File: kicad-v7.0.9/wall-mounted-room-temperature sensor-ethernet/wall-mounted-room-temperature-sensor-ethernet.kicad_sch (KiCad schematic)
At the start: 165 parts, among them J1 54601-908WPLF, P1 2x3_MLW06A, P2 DS1023-1-9S21, Q1 DMG2307L, Q2 FDC2512, SW1 TVAF18BB, SW2 TVAF18BB, SW3 B3F-4150, SW4 B3F-4150, SW5 B3F-4150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

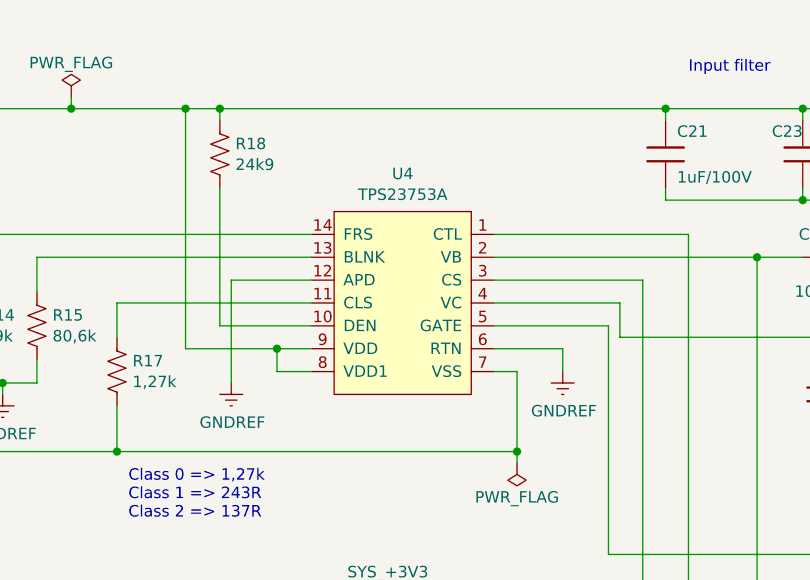
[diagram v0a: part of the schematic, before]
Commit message: Change components form library. Adding of BOM.
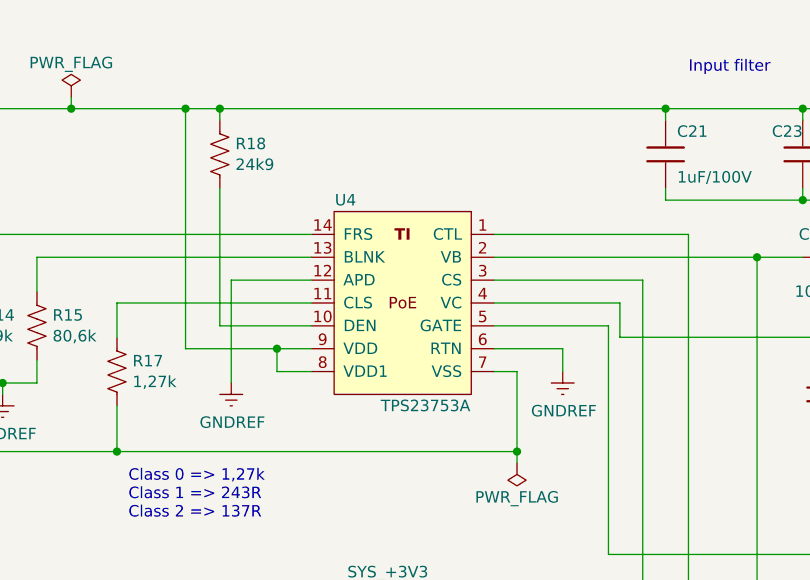
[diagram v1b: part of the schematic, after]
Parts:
- P1: footprint connector_idc_rl:2x3_MLW06A -> connector_idc_tht_rl:2x3_MLW06A; symbol connector_idc_rl:2x3_MLW06A -> connector_idc_tht_rl:2x3_MLW06A
- P2: footprint connector_tht_pinsocket_2.54mm_rl:1x9_pinsocket_2.54mm_vertical_8.5mm -> connector_pin_socket_2.54mm_tht_rl:1x9_pin_socket_2.54mm_vertical_8.5mm; symbol connector_tht_pin_socket_2.54mm_rl:DS1023-1-9S21 -> connector_pin_socket_2.54mm_tht_rl:DS1023-1-9S21
- U4: symbol poe_interface_isolated_converter_rl:TPS23753A -> poe_interface_isolated_converter_rl:TPS23753APW
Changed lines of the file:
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@@
     (effects (font (size 1.27 1.27)) (justify left bottom))
   )
-  (symbol (lib_id "poe_interface_isolated_converter_rl:TPS23753A") (at 168.91 57.15 0) (mirror y) (unit 1)
+  (symbol (lib_id "poe_interface_isolated_converter_rl:TPS23753APW") (at 168.91 57.15 0) (mirror y) (unit 1)
     (in_bom yes) (on_board yes) (dnp no)
-    (property "Reference" "U4" (at 168.91 40.259 0)
+    (property "Reference" "U4" (at 162.56 43.18 0)
       (effects (font (size 1.27 1.27)))
     )
-    (property "Value" "TPS23753A" (at 168.91 42.5704 0)
+    (property "Value" "TPS23753A" (at 171.45 66.04 0)
       (effects (font (size 1.27 1.27)))
     )
-    (property "Footprint" "package_tssop_rl:tssop_14" (at 168.91 57.15 0)
+    (property "Footprint" "package_tssop_rl:tssop_14" (at 168.91 38.1 0)
       (effects (font (size 1.27 1.27)) hide)
     )
-    (property "Datasheet" "https://www.ti.com/lit/gpn/tps23753a" (at 168.91 57.15 0)
+    (property "Datasheet" "https://www.ti.com/lit/gpn/tps23753a" (at 168.91 40.64 0)
       (effects (font (size 1.27 1.27)) hide)
     )
@@
     )
   )
-  (symbol (lib_id "connector_idc_rl:2x3_MLW06A") (at 350.52 335.28 0) (mirror x) (unit 1)
+  (symbol (lib_id "connector_idc_tht_rl:2x3_MLW06A") (at 350.52 335.28 0) (mirror x) (unit 1)
     (in_bom yes) (on_board yes) (dnp no)
     (property "Reference" "P1" (at 345.9734 334.7466 0)
@@
       (effects (font (size 1.27 1.27)))
     )
-    (property "Footprint" "connector_idc_rl:2x3_MLW06A" (at 350.52 351.79 0)
+    (property "Footprint" "connector_idc_tht_rl:2x3_MLW06A" (at 350.52 351.79 0)
       (effects (font (size 1.27 1.27)) hide)
     )
@@
     )
   )
-  (symbol (lib_id "connector_tht_pin_socket_2.54mm_rl:DS1023-1-9S21") (at 403.86 250.19 0) (mirror y) (unit 1)
+  (symbol (lib_id "connector_pin_socket_2.54mm_tht_rl:DS1023-1-9S21") (at 403.86 250.19 0) (mirror y) (unit 1)
     (in_bom yes) (on_board yes) (dnp no)
     (property "Reference" "P2" (at 403.86 245.11 0)
@@
       (effects (font (size 1.27 1.27)))
     )
-    (property "Footprint" "connector_tht_pinsocket_2.54mm_rl:1x9_pinsocket_2.54mm_vertical_8.5mm" (at 403.86 242.57 0)
+    (property "Footprint" "connector_pin_socket_2.54mm_tht_rl:1x9_pin_socket_2.54mm_vertical_8.5mm" (at 403.86 242.57 0)
       (effects (font (size 1.27 1.27)) hide)
     )
